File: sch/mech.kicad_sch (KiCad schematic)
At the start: 7 parts, among them J3 FBA_ESD_strip_bottom, K2 Key_K1_K2_TE_1-1469373-1

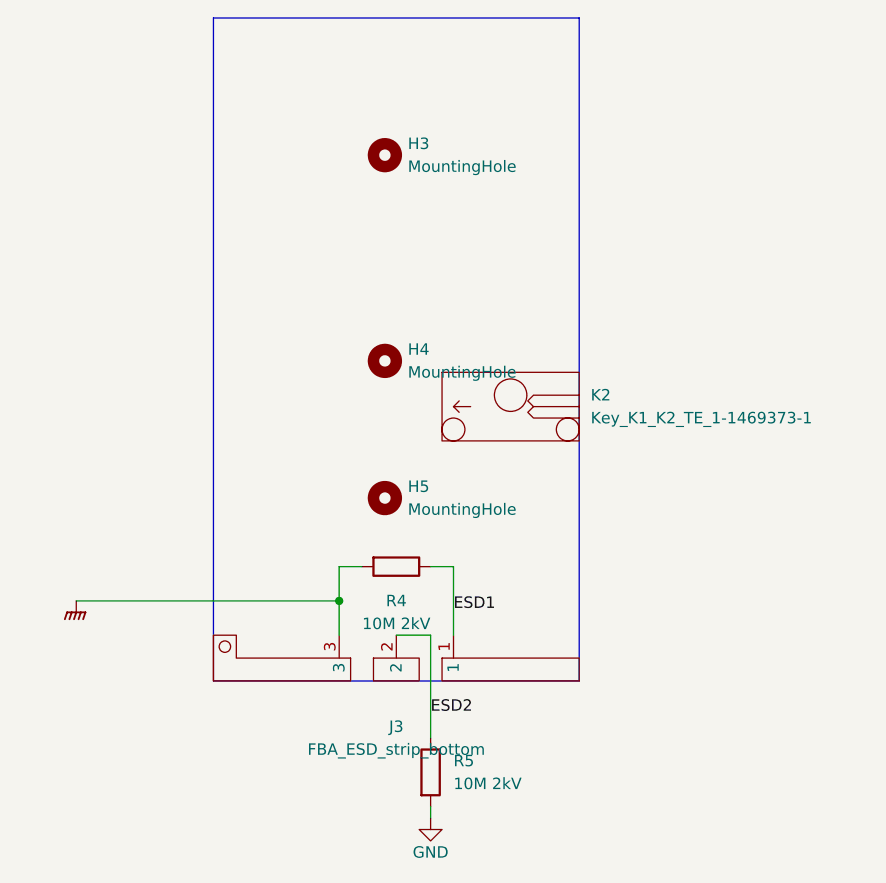
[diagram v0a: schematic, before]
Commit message: added magjacks
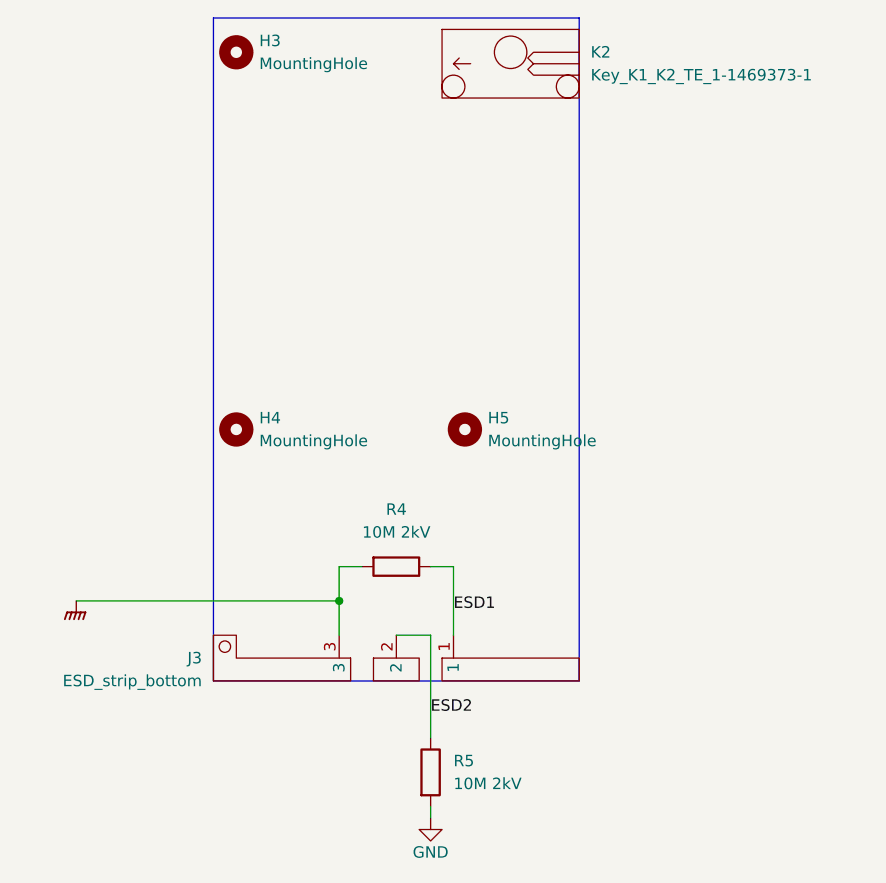
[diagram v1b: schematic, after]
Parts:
- H3, H4, H5: footprint KIT_Mechanical:NPTH_2.7_7_Keepout -> project:NPTH_2.7_7_Keepout
- J3: value FBA_ESD_strip_bottom -> ESD_strip_bottom; footprint KIT_Mechanical:FBA_ESD_strip_bottom -> project:ESD_strip_bottom
- K2: footprint KIT_Mechanical:Key_K1_K2_TE_1-1469373-1 -> project:Key_K1_K2_TE_1-1469373-1
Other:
- moved on the sheet: H3, H4, H5, K2
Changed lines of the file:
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@@
     )
   )
-  (symbol (lib_id "Mechanical:MountingHole") (at 161.29 67.31 0) (unit 1)
+  (symbol (lib_id "Mechanical:MountingHole") (at 144.78 55.88 0) (unit 1)
     (in_bom yes) (on_board yes) (dnp no) (fields_autoplaced)
-    (property "Reference" "H3" (at 163.83 66.0399 0)
+    (property "Reference" "H3" (at 147.32 54.6099 0)
       (effects (font (size 1.27 1.27)) (justify left))
     )
-    (property "Value" "MountingHole" (at 163.83 68.5799 0)
+    (property "Value" "MountingHole" (at 147.32 57.1499 0)
       (effects (font (size 1.27 1.27)) (justify left))
     )
-    (property "Footprint" "KIT_Mechanical:NPTH_2.7_7_Keepout" (at 161.29 67.31 0)
+    (property "Footprint" "project:NPTH_2.7_7_Keepout" (at 144.78 55.88 0)
       (effects (font (size 1.27 1.27)) hide)
     )
-    (property "Datasheet" "~" (at 161.29 67.31 0)
+    (property "Datasheet" "~" (at 144.78 55.88 0)
       (effects (font (size 1.27 1.27)) hide)
     )
-    (property "stock" "PCB" (at 161.29 67.31 0)
+    (property "stock" "PCB" (at 144.78 55.88 0)
       (effects (font (size 1.27 1.27)) hide)
     )
@@
     )
   )
-  (symbol (lib_id "Mechanical:MountingHole") (at 161.29 90.17 0) (unit 1)
+  (symbol (lib_id "Mechanical:MountingHole") (at 144.78 97.79 0) (unit 1)
     (in_bom yes) (on_board yes) (dnp no) (fields_autoplaced)
-    (property "Reference" "H4" (at 163.83 88.8999 0)
+    (property "Reference" "H4" (at 147.32 96.5199 0)
       (effects (font (size 1.27 1.27)) (justify left))
     )
-    (property "Value" "MountingHole" (at 163.83 91.4399 0)
+    (property "Value" "MountingHole" (at 147.32 99.0599 0)
       (effects (font (size 1.27 1.27)) (justify left))
     )
-    (property "Footprint" "KIT_Mechanical:NPTH_2.7_7_Keepout" (at 161.29 90.17 0)
+    (property "Footprint" "project:NPTH_2.7_7_Keepout" (at 144.78 97.79 0)
       (effects (font (size 1.27 1.27)) hide)
     )
-    (property "Datasheet" "~" (at 161.29 90.17 0)
+    (property "Datasheet" "~" (at 144.78 97.79 0)
       (effects (font (size 1.27 1.27)) hide)
     )
-    (property "stock" "PCB" (at 161.29 90.17 0)
+    (property "stock" "PCB" (at 144.78 97.79 0)
       (effects (font (size 1.27 1.27)) hide)
     )
@@
     )
   )
-  (symbol (lib_id "project:Key_K1_K2_TE_1-1469373-1") (at 175.26 95.25 0) (unit 1)
+  (symbol (lib_id "project:Key_K1_K2_TE_1-1469373-1") (at 175.26 57.15 0) (unit 1)
     (in_bom yes) (on_board yes) (dnp no) (fields_autoplaced)
-    (property "Reference" "K2" (at 184.15 93.98 0)
+    (property "Reference" "K2" (at 184.15 55.88 0)
       (effects (font (size 1.27 1.27)) (justify left))
     )
-    (property "Value" "Key_K1_K2_TE_1-1469373-1" (at 184.15 96.52 0)
+    (property "Value" "Key_K1_K2_TE_1-1469373-1" (at 184.15 58.42 0)
       (effects (font (size 1.27 1.27)) (justify left))
     )
-    (property "Footprint" "KIT_Mechanical:Key_K1_K2_TE_1-1469373-1" (at 172.72 88.9 0)
+    (property "Footprint" "project:Key_K1_K2_TE_1-1469373-1" (at 172.72 50.8 0)
       (effects (font (size 1.27 1.27)) hide)
     )
-    (property "Datasheet" "https://www.te.com/commerce/DocumentDelivery/DDEController?Action=showdoc&DocId=Customer+Drawing%7F1469373%7FE1%7Fpdf%7FEnglish%7FENG_CD_1469373_E1.pdf%7F1-1469373-1" (at 167.64 93.98 0)
+    (property "Datasheet" "https://www.te.com/commerce/DocumentDelivery/DDEController?Action=showdoc&DocId=Customer+Drawing%7F1469373%7FE1%7Fpdf%7FEnglish%7FENG_CD_1469373_E1.pdf%7F1-1469373-1" (at 167.64 55.88 0)
       (effects (font (size 1.27 1.27)) hide)
     )
-    (property "rs#" "718-1418" (at 173.99 102.87 0)
+    (property "rs#" "718-1418" (at 173.99 64.77 0)
       (effects (font (size 1.27 1.27)) hide)
     )
-    (property "manf" "TE Connectivity" (at 173.99 101.6 0)
+    (property "manf" "TE Connectivity" (at 173.99 63.5 0)
       (effects (font (size 1.27 1.27)) hide)
     )
-    (property "manf#" "1-1469373-1" (at 173.99 105.41 0)
+    (property "manf#" "1-1469373-1" (at 173.99 67.31 0)
       (effects (font (size 1.27 1.27)) hide)
     )
-    (property "digikey#" "1-1469373-1-ND" (at 175.26 95.25 0)
+    (property "digikey#" "1-1469373-1-ND" (at 175.26 57.15 0)
       (effects (font (size 1.27 1.27)) hide)
     )
-    (property "stock" "Box: 11" (at 175.26 95.25 0)
+    (property "stock" "Box: 11" (at 175.26 57.15 0)
       (effects (font (size 1.27 1.27)) hide)
     )
@@
     )
   )
-  (symbol (lib_id "Mechanical:MountingHole") (at 161.29 105.41 0) (unit 1)
+  (symbol (lib_id "Mechanical:MountingHole") (at 170.18 97.79 0) (unit 1)
     (in_bom yes) (on_board yes) (dnp no) (fields_autoplaced)
-    (property "Reference" "H5" (at 163.83 104.1399 0)
+    (property "Reference" "H5" (at 172.72 96.5199 0)
       (effects (font (size 1.27 1.27)) (justify left))
     )
-    (property "Value" "MountingHole" (at 163.83 106.6799 0)
+    (property "Value" "MountingHole" (at 172.72 99.0599 0)
       (effects (font (size 1.27 1.27)) (justify left))
     )
-    (property "Footprint" "KIT_Mechanical:NPTH_2.7_7_Keepout" (at 161.29 105.41 0)
+    (property "Footprint" "project:NPTH_2.7_7_Keepout" (at 170.18 97.79 0)
       (effects (font (size 1.27 1.27)) hide)
     )
-    (property "Datasheet" "~" (at 161.29 105.41 0)
+    (property "Datasheet" "~" (at 170.18 97.79 0)
       (effects (font (size 1.27 1.27)) hide)
     )
-    (property "stock" "PCB" (at 161.29 105.41 0)
+    (property "stock" "PCB" (at 170.18 97.79 0)
       (effects (font (size 1.27 1.27)) hide)
     )
@@
   (symbol (lib_id "Device:R") (at 162.56 113.03 270) (unit 1)
     (in_bom yes) (on_board yes) (dnp no) (fields_autoplaced)
-    (property "Reference" "R4" (at 162.56 116.84 90)
+    (property "Reference" "R4" (at 162.56 106.68 90)
       (effects (font (size 1.27 1.27)))
     )
-    (property "Value" "10M 2kV" (at 162.56 119.38 90)
+    (property "Value" "10M 2kV" (at 162.56 109.22 90)
       (effects (font (size 1.27 1.27)))
     )
@@
   (symbol (lib_id "project:FBA_ESD_strip_bottom") (at 162.56 123.19 0) (unit 1)
     (in_bom no) (on_board yes) (dnp no) (fields_autoplaced)
-    (property "Reference" "J3" (at 162.56 130.81 0)
-      (effects (font (size 1.27 1.27)))
+    (property "Reference" "J3" (at 140.97 123.19 0)
+      (effects (font (size 1.27 1.27)) (justify right))
     )
-    (property "Value" "FBA_ESD_strip_bottom" (at 162.56 133.35 0)
-      (effects (font (size 1.27 1.27)))
+    (property "Value" "ESD_strip_bottom" (at 140.97 125.73 0)
+      (effects (font (size 1.27 1.27)) (justify right))
     )
-    (property "Footprint" "KIT_Mechanical:FBA_ESD_strip_bottom" (at 162.56 123.19 0)
+    (property "Footprint" "project:ESD_strip_bottom" (at 162.56 123.19 0)
       (effects (font (size 1.27 1.27)) hide)
     )

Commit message: Project recovered
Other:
- title: ATCA Template -> ATCA Simple Loopback HUB
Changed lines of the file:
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@@
   (paper "A4")
   (title_block
-    (title "ATCA Template")
-    (date "2023-07-20")
+    (title "ATCA Simple Loopback HUB")
+    (date "2023-09-12")
     (rev "1.0")
     (company "Karlsruhe Institute of Technology (KIT)")
     (comment 1 "Institute for Data Processing and Electronics (IPE)")
     (comment 2 "Luis Ardila")
-    (comment 4 "Licensed under CERN-OHL-S-2.0")
+    (comment 3 "IPE-380-06")
+    (comment 4 "Licensed under CERN-OHL-P-2.0")
   )
   (junction (at 156.21 116.84) (diameter 0) (color 0 0 0 0)
@@
     (pin "1")
     (instances
-      (project "atca_simple_hub"
+      (project "atca-simple-loopback-hub"
         (path "/b1bf14e0-f6d2-45a7-b67f-6500a354b7ad/f77876dd-ebdc-4e20-8c96-1773c09aca35"
           (reference "#PWR011") (unit 1)
@@
     (pin "2")
     (instances
-      (project "atca_simple_hub"
+      (project "atca-simple-loopback-hub"
         (path "/b1bf14e0-f6d2-45a7-b67f-6500a354b7ad/f77876dd-ebdc-4e20-8c96-1773c09aca35"
           (reference "R5") (unit 1)
@@
     )
     (instances
-      (project "atca_simple_hub"
+      (project "atca-simple-loopback-hub"
         (path "/b1bf14e0-f6d2-45a7-b67f-6500a354b7ad/f77876dd-ebdc-4e20-8c96-1773c09aca35"
           (reference "H3") (unit 1)
@@
     )
     (instances
-      (project "atca_simple_hub"
+      (project "atca-simple-loopback-hub"
         (path "/b1bf14e0-f6d2-45a7-b67f-6500a354b7ad/f77876dd-ebdc-4e20-8c96-1773c09aca35"
           (reference "H4") (unit 1)
@@
     )
     (instances
-      (project "atca_simple_hub"
+      (project "atca-simple-loopback-hub"
         (path "/b1bf14e0-f6d2-45a7-b67f-6500a354b7ad/f77876dd-ebdc-4e20-8c96-1773c09aca35"
           (reference "K2") (unit 1)
@@
     )
     (instances
-      (project "atca_simple_hub"
+      (project "atca-simple-loopback-hub"
         (path "/b1bf14e0-f6d2-45a7-b67f-6500a354b7ad/f77876dd-ebdc-4e20-8c96-1773c09aca35"
           (reference "H5") (unit 1)
@@
     (pin "2")
     (instances
-      (project "atca_simple_hub"
+      (project "atca-simple-loopback-hub"
         (path "/b1bf14e0-f6d2-45a7-b67f-6500a354b7ad/f77876dd-ebdc-4e20-8c96-1773c09aca35"
           (reference "R4") (unit 1)
@@
     (pin "3")
     (instances
-      (project "atca_simple_hub"
+      (project "atca-simple-loopback-hub"
         (path "/b1bf14e0-f6d2-45a7-b67f-6500a354b7ad/f77876dd-ebdc-4e20-8c96-1773c09aca35"
           (reference "J3") (unit 1)
@@
     (pin "1")
     (instances
-      (project "atca_simple_hub"
+      (project "atca-simple-loopback-hub"
         (path "/b1bf14e0-f6d2-45a7-b67f-6500a354b7ad/f77876dd-ebdc-4e20-8c96-1773c09aca35"
           (reference "#PWR013") (unit 1)

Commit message: BI and FI
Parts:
- H3, H4, H5: symbol Mechanical:MountingHole -> project:MountingHole
- R4, R5: symbol Device:R -> project:R
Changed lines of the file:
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@@
     )
   )
-  (symbol (lib_id "Device:R") (at 166.37 135.89 0) (unit 1)
+  (symbol (lib_id "project:R") (at 166.37 135.89 0) (unit 1)
     (in_bom yes) (on_board yes) (dnp no) (fields_autoplaced)
     (property "Reference" "R5" (at 168.91 134.6199 0)
@@
     )
   )
-  (symbol (lib_id "Mechanical:MountingHole") (at 144.78 55.88 0) (unit 1)
+  (symbol (lib_id "project:MountingHole") (at 144.78 55.88 0) (unit 1)
     (in_bom yes) (on_board yes) (dnp no) (fields_autoplaced)
     (property "Reference" "H3" (at 147.32 54.6099 0)
@@
     )
   )
-  (symbol (lib_id "Mechanical:MountingHole") (at 144.78 97.79 0) (unit 1)
+  (symbol (lib_id "project:MountingHole") (at 144.78 97.79 0) (unit 1)
     (in_bom yes) (on_board yes) (dnp no) (fields_autoplaced)
     (property "Reference" "H4" (at 147.32 96.5199 0)
@@
     )
   )
-  (symbol (lib_id "Mechanical:MountingHole") (at 170.18 97.79 0) (unit 1)
+  (symbol (lib_id "project:MountingHole") (at 170.18 97.79 0) (unit 1)
     (in_bom yes) (on_board yes) (dnp no) (fields_autoplaced)
     (property "Reference" "H5" (at 172.72 96.5199 0)
@@
     )
   )
-  (symbol (lib_id "Device:R") (at 162.56 113.03 270) (unit 1)
+  (symbol (lib_id "project:R") (at 162.56 113.03 270) (unit 1)
     (in_bom yes) (on_board yes) (dnp no) (fields_autoplaced)
     (property "Reference" "R4" (at 162.56 106.68 90)

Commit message: sfp+ sheet
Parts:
- renumbered R4 to R11, R5 to R12
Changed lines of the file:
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@@
   (symbol (lib_id "project:R") (at 166.37 135.89 0) (unit 1)
     (in_bom yes) (on_board yes) (dnp no) (fields_autoplaced)
-    (property "Reference" "R5" (at 168.91 134.6199 0)
+    (property "Reference" "R12" (at 168.91 134.62 0)
       (effects (font (size 1.27 1.27)) (justify left))
     )
-    (property "Value" "10M 2kV" (at 168.91 137.1599 0)
+    (property "Value" "10M 2kV" (at 168.91 137.16 0)
       (effects (font (size 1.27 1.27)) (justify left))
     )
@@
       (project "atca-simple-loopback-hub"
         (path "/b1bf14e0-f6d2-45a7-b67f-6500a354b7ad/f77876dd-ebdc-4e20-8c96-1773c09aca35"
-          (reference "R5") (unit 1)
+          (reference "R12") (unit 1)
         )
       )
@@
   (symbol (lib_id "project:R") (at 162.56 113.03 270) (unit 1)
     (in_bom yes) (on_board yes) (dnp no) (fields_autoplaced)
-    (property "Reference" "R4" (at 162.56 106.68 90)
+    (property "Reference" "R11" (at 162.56 106.68 90)
       (effects (font (size 1.27 1.27)))
     )
@@
       (project "atca-simple-loopback-hub"
         (path "/b1bf14e0-f6d2-45a7-b67f-6500a354b7ad/f77876dd-ebdc-4e20-8c96-1773c09aca35"
-          (reference "R4") (unit 1)
+          (reference "R11") (unit 1)
         )
       )

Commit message: sch work
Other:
- note added: "add other KEY and standard mounting holes add front panel"
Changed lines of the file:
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@@
   (title_block
     (title "ATCA Simple Loopback HUB")
-    (date "2023-09-12")
+    (date "2023-09-26")
     (rev "1.0")
     (company "Karlsruhe Institute of Technology (KIT)")
@@
     (stroke (width 0) (type default))
   )
+  (wire (pts (xy 127 116.84) (xy 127 118.11))
+    (stroke (width 0) (type default))
+  )
+  (text "add other KEY and standard mounting holes\nadd front panel\n"
+    (at 76.2 41.91 0)
+    (effects (font (size 5 5)) (justify left bottom))
+  )
   (label "ESD2" (at 166.37 129.54 0) (fields_autoplaced)
     (effects (font (size 1.27 1.27)) (justify left bottom))
@@
     (effects (font (size 1.27 1.27)) (justify left bottom))
   )
-  (symbol (lib_id "power:GNDPWR") (at 127 116.84 0) (unit 1)
-    (in_bom yes) (on_board yes) (dnp no)
-    (property "Reference" "#PWR011" (at 127 121.92 0)
-      (effects (font (size 1.27 1.27)) hide)
-    )
-    (property "Value" "~" (at 127.1016 120.7516 0)
-      (effects (font (size 1.27 1.27)))
-    )
-    (property "Footprint" "" (at 127 118.11 0)
-      (effects (font (size 1.27 1.27)) hide)
-    )
-    (property "Datasheet" "" (at 127 118.11 0)
-      (effects (font (size 1.27 1.27)) hide)
-    )
-    (pin "1")
-    (instances
-      (project "atca-simple-loopback-hub"
-        (path "/b1bf14e0-f6d2-45a7-b67f-6500a354b7ad/f77876dd-ebdc-4e20-8c96-1773c09aca35"
-          (reference "#PWR011") (unit 1)
-        )
-      )
-    )
-  )
   (symbol (lib_id "project:R") (at 166.37 135.89 0) (unit 1)
     (in_bom yes) (on_board yes) (dnp no) (fields_autoplaced)
@@
     )
   )
+  (symbol (lib_id "power:GNDPWR") (at 127 118.11 0) (unit 1)
+    (in_bom yes) (on_board yes) (dnp no) (fields_autoplaced)
+    (property "Reference" "#PWR074" (at 127 123.19 0)
+      (effects (font (size 1.27 1.27)) hide)
+    )
+    (property "Value" "GNDPWR" (at 126.873 121.92 0)
+      (effects (font (size 1.27 1.27)))
+    )
+    (property "Footprint" "" (at 127 119.38 0)
+      (effects (font (size 1.27 1.27)) hide)
+    )
+    (property "Datasheet" "" (at 127 119.38 0)
+      (effects (font (size 1.27 1.27)) hide)
+    )
+    (pin "1")
+    (instances
+      (project "atca-simple-loopback-hub"
+        (path "/b1bf14e0-f6d2-45a7-b67f-6500a354b7ad/f77876dd-ebdc-4e20-8c96-1773c09aca35"
+          (reference "#PWR074") (unit 1)
+        )
+      )
+    )
+  )
   (symbol (lib_id "project:FBA_ESD_strip_bottom") (at 162.56 123.19 0) (unit 1)
-    (in_bom no) (on_board yes) (dnp no) (fields_autoplaced)
+    (in_bom no) (on_board yes) (dnp no)
     (property "Reference" "J3" (at 140.97 123.19 0)
       (effects (font (size 1.27 1.27)) (justify right))
     )
-    (property "Value" "ESD_strip_bottom" (at 140.97 125.73 0)
+    (property "Value" "ESD_strip_bottom" (at 156.21 127 0)
       (effects (font (size 1.27 1.27)) (justify right))
     )

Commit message: before sch review
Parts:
- added A1: FrontPanel, KIT_Mechanical:FrontPanel, symbol KIT_Mechanical:FrontPanel
- added H1: 81-088-1, KIT_Mechanical:81-301-00, symbol KIT_Switch:Handle_81-088-1
- added H2: Handle, project:81-300-00, symbol KIT_Switch:Handle
- added J12: Conn_01x03_Male, KIT_Connector:Molex_53046-0310, symbol Connector:Conn_01x03_Male
- added K1: Key_K1_K2_TE_1-1469373-1, project:Key_K1_K2_TE_1-1469373-1, symbol project:Key_K1_K2_TE_1-1469373-1
- added R148: 10k, Resistor_SMD:R_0603_1608Metric, symbol Device:R
- J3: footprint project:ESD_strip_bottom -> project:ESD_Strip; stock PCB -> (none)
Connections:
- net GND: now also J12.2 (Pin_2)
- new net +3V3_STBY: R148.1
- new net FP_HANDLE: J12.1 (Pin_1), R148.2
- no-connect marks 0 -> 1
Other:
- note added: "Insert: 3V3 -> GND Remove: GND -> 3V3"
- moved on the sheet: H3, H4, H5, K2

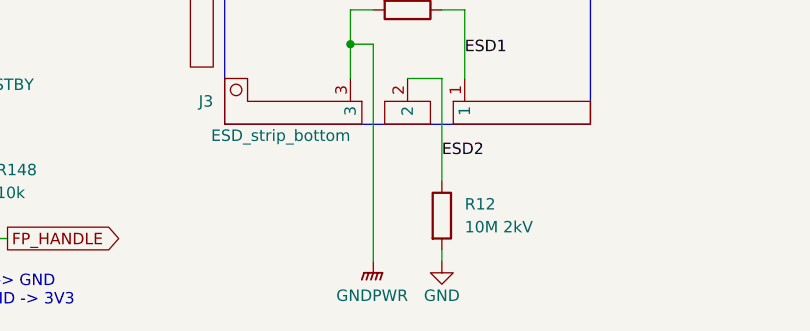
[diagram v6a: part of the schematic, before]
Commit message: started changes from review
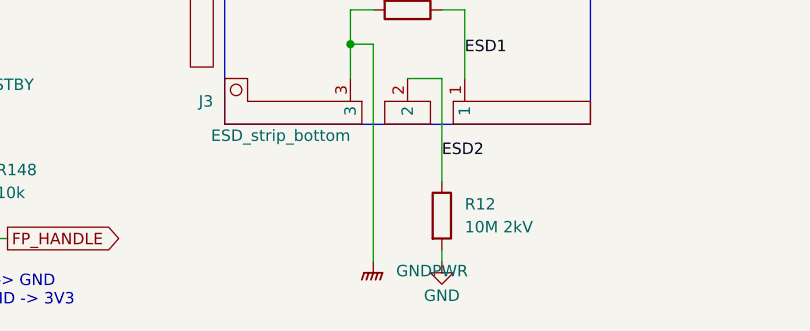
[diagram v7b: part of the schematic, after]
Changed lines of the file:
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@@
       (effects (font (size 1.27 1.27)) hide)
     )
-    (property "Value" "GNDPWR" (at 158.623 144.78 0)
-      (effects (font (size 1.27 1.27)))
+    (property "Value" "GNDPWR" (at 161.29 142.0368 0)
+      (effects (font (size 1.27 1.27)) (justify left))
     )
     (property "Footprint" "" (at 158.75 142.24 0)

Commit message: starting doing stackup calculations
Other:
- note removed: "add other KEY and standard mounting holes add front panel"
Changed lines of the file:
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@@
     (stroke (width 0) (type default))
-  )
-  (text "add other KEY and standard mounting holes\nadd front panel\n"
-    (at 72.39 -2.54 0)
-    (effects (font (size 5 5)) (justify left bottom))
   )
   (text "Insert: 3V3 -> GND\nRemove: GND -> 3V3" (at 106.68 146.05 0)
